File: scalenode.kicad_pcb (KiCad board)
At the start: 4 copper layers, 173.5 x 40 mm, 159 parts, among them IC2 TPS2378DDA, J3 1-2199230-6, J4 1140084168, J5 0473460001, J6 SS-74800-144, J7 DF40HC(3.0)-100DS-0.4v, J8 DF40HC(3.0)-100DS-0.4v, M1 compute-module-4-1.5mm, Q1 MMBT3906,215, Q2 MMBT3906,215, Q3 SI7848BDP-T1-E3, Q4 SI7450DP-T1-GE3, Q5 MMBT3906,215, T1 P0926NL, T2 POE300F-50L, U1 TS3USB30EDGSR, U2 TPS62823DLCT, U3 UCC3809D2, U4 TCMT1107

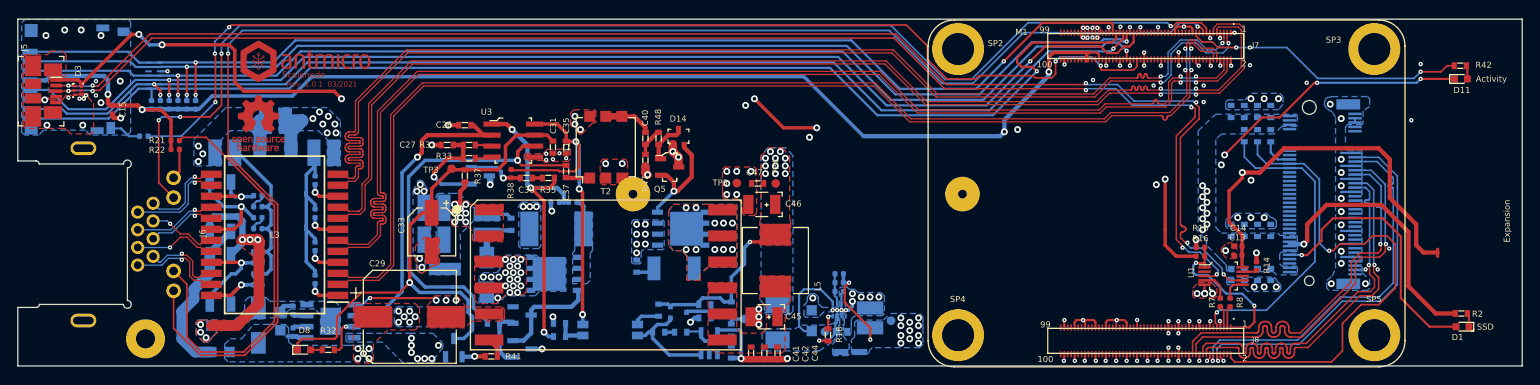
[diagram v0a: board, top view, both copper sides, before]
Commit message: Moved CM4 board, rerouted power
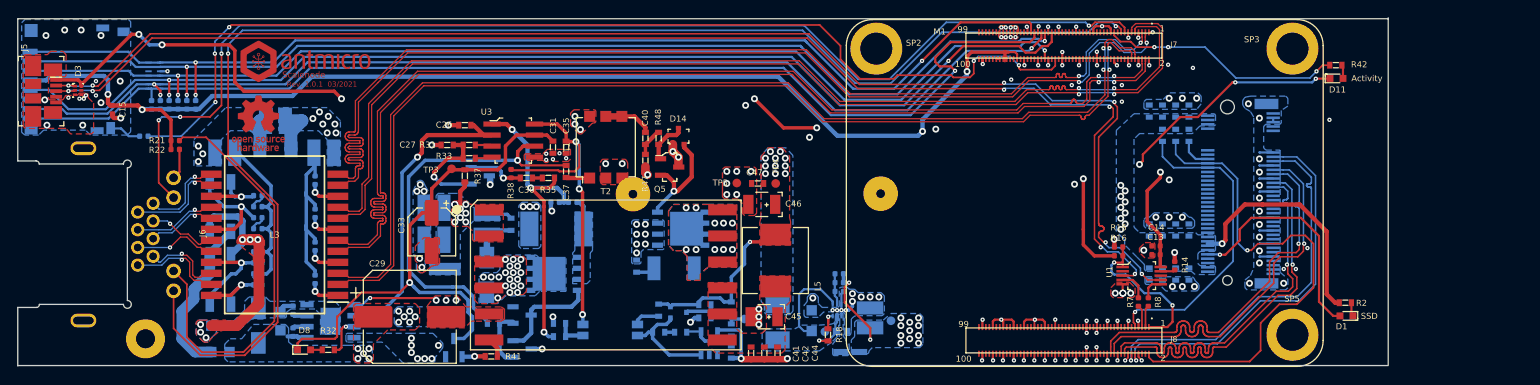
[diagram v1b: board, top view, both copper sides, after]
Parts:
- removed SP4: 9774030151, scalenode-footprints:9774030151
- moved D11 14.4 mm to (189.2, 63.4)
- moved R42 14.4 mm to (189.1, 61.9)
- moved D1 13.4 mm to (190.3, 90.8)
- moved R2 13.4 mm to (190.2, 89.3)
- moved C13 9.44 mm to (168.4, 83.8)
- moved C14 9.44 mm to (168.4, 82.8)
- moved M1 9.44 mm to (154.6, 56.1)
- moved R14 9.44 mm to (170.5, 85.0)
- moved R15 9.44 mm to (164.0, 82.9)
- moved R16 9.44 mm to (164.0, 83.9)
- moved R7 9.44 mm to (166.3, 89.2)
- moved R8 9.44 mm to (167.5, 89.2)
- moved SP2 9.44 mm to (136.1, 60.1)
- moved SP3 9.44 mm to (184.1, 60.1)
- moved SP5 9.44 mm to (184.1, 93.1)
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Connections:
- D3 pad 6: /Interfaces/VBus_Slave -> 3V3_RPi
- J5 pad 1: /Interfaces/VBus_Slave -> 3V3_RPi
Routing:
- net /Interfaces/VBus_Slave: track 152.7 -> 11.7 mm, vias 6 -> 1
- net 3V3_RPi: track 251.8 -> 317.3 mm, vias 8 -> 14
- net /Interfaces/RPi_USB_P: track 163.2 -> 153.8 mm
- net TRD3_P: track 131.7 -> 122.3 mm
- net TRD2_P: track 131.6 -> 122.2 mm
- net SD_CLK: track 140.1 -> 130.7 mm
- net /Interfaces/RPi_USB_N: track 165.6 -> 156.2 mm
- net TRD0_P: track 131.7 -> 122.3 mm
- net TRD3_N: track 131.7 -> 122.3 mm
- net SD_DAT1: track 140.5 -> 131.1 mm
- net SD_CMD: track 137.2 -> 127.8 mm
- net ETH_LEDG: track 145.6 -> 136.1 mm
- net TRD1_N: track 131.7 -> 122.3 mm
- net SD_DAT0: track 137.3 -> 127.9 mm
- net ETH_LEDY: track 172.8 -> 163.4 mm
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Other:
- board size 173.5 x 40 mm -> 158.1 x 40.2 mm
- board text removed: "Expansion"
